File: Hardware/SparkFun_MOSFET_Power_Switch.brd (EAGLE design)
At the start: 38.1 x 35.6 mm, 75 parts, among them J1 PTH, J3 5.5x2.1mm Barrel, J4 SMD, Q1 600mA/40V, Q2 100A/100V/6.8mΩ, U1 LMR14203

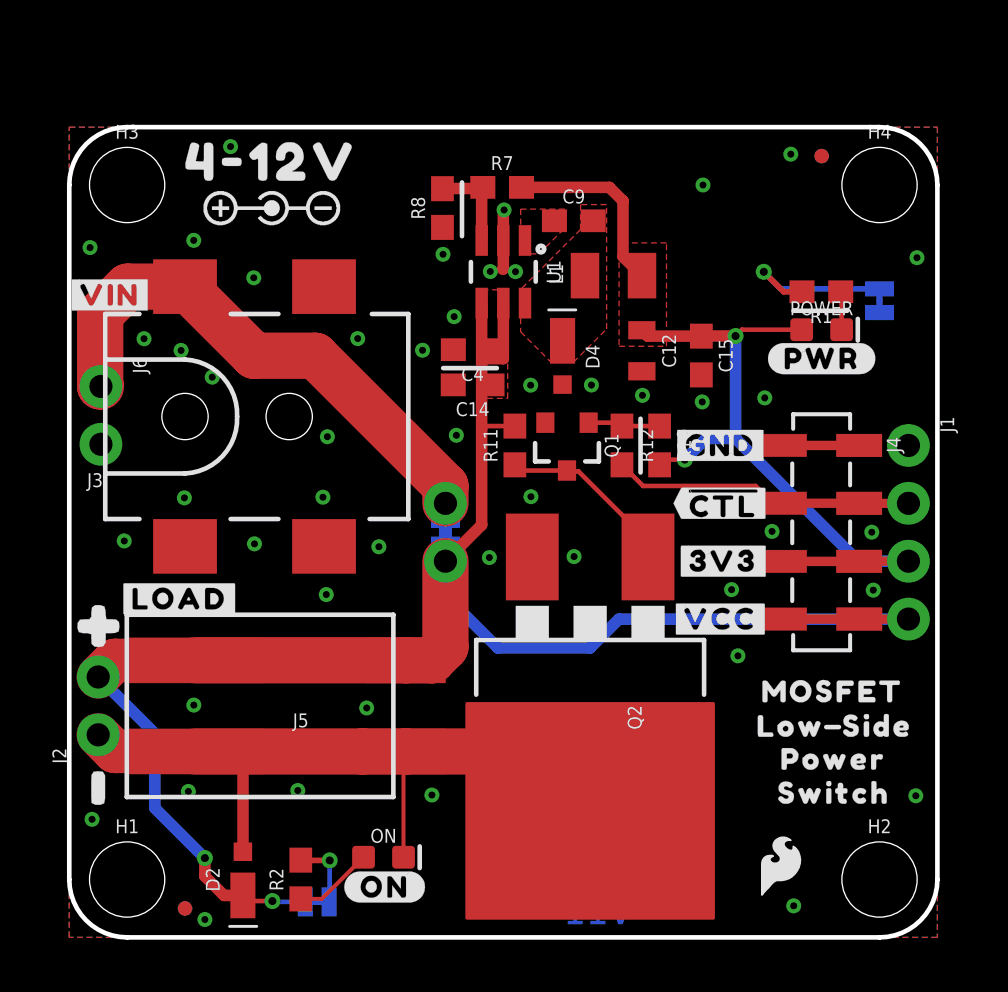
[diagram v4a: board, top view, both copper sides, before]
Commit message: Group Review mods round one
-Powered ON LED from 3.3V and controlled via CTL net.
-Moved GND/VIN PTH headers away from under the barrel jack for easier access
-routed some of load path with polygons to avoid sharp 90 degree turns in traces
-moved MEAS jumper to allow direct GND pour path from MOSFET to Barrel jack GND pads
-added "+" and "-" silk to MEAS jumper PTH header
-enlarged board to 1.5" square shape
-spaced out components near BJT for better DFM
-nudged some vias to avoid silk
-corrected voltage input range to "4.5-12V".
-added ordering instructions
-Larger logos
-added and updated measures
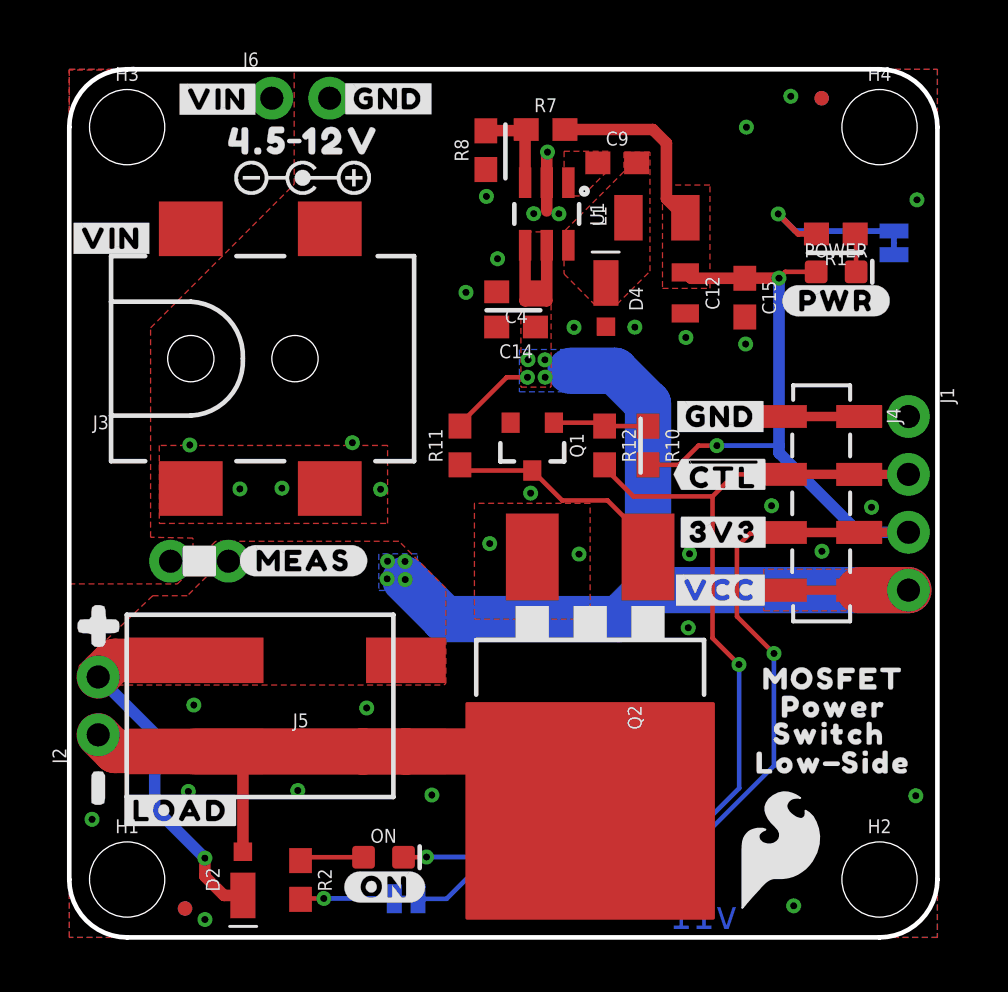
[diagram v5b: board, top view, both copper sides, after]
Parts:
- added LOGO3: SPECIAL_INSTRUCTIONS-ORDERING, SparkFun-Aesthetics:ORDERING_INSTRUCTIONS
- added U$18: (no value), output:4#5_12V5
- added U$21: (no value), output:#VIN#8
- added U$38: (no value), output:#MEAS#14
- LOGO1: value OSHW-LOGOS -> OSHW-LOGOM; device SparkFun-Aesthetics:OSHW-LOGO-S -> SparkFun-Aesthetics:OSHW-LOGO-M
- LOGO2: value SFE_LOGO_NAME_FLAME.1_INCH -> SFE_LOGO_NAME_FLAME.2_INCH; device SparkFun-Aesthetics:SFE_LOGO_NAME_FLAME_.1 -> SparkFun-Aesthetics:SFE_LOGO_NAME_FLAME_.2
- U$6: device output:4#12V0 -> output:#GND#0
- U$8: device SparkFun-Aesthetics:SFE_LOGO_FLAME_.1 -> SparkFun-Aesthetics:SFE_LOGO_FLAME_.2
- moved U$37 18.3 mm to (11.4, 34.3)
- moved U$34 15.1 mm to (15.7, 11.8)
- moved U$35 15.1 mm to (22.1, 11.9)
- moved J6 14.7 mm to (8.89, 36.8), turned to 0 degrees
- moved U$36 11.1 mm to (8.89, 34.5)
- moved MEAS 10.9 mm to (5.71, 16.5), turned to 180 degrees
- moved U$24 10.4 mm to (18.5, 18.7)
- moved LOGO2 9.52 mm to (18.8, 21.9)
- moved U$1 9.29 mm to (4.87, 5.57)
- moved U$17 9.17 mm to (5.74, 18.2), turned to 0 degrees
- moved U$26 8.26 mm to (18.8, 14.2)
- moved U$25 8.24 mm to (18.7, 16.6)
- moved LOGO1 5.92 mm to (33.9, 8.56)
- moved U$6 5.82 mm to (14.0, 36.8)
- moved U$16 3.95 mm to (19.4, 1.66)
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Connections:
- net !CTL: now also ON.C
- net 3.3V: now also ON_LED.2
- net LOAD: no longer ON.C
- net VCC: no longer ON_LED.2
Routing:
- net 3.3V: track 35.8 -> 73.5 mm, vias 2 -> 3
- net !CTL: track 15.4 -> 43.7 mm, vias 0 -> 2
- net VIN: track 24.0 -> 0.76 mm
- net VCC: track 78.2 -> 66.6 mm, vias 2 -> 9
- net LOAD: track 33.1 -> 28.4 mm
- net N$1: track 7.93 -> 10.3 mm
- net N$7: track 3.11 -> 4.14 mm
- net N$12: track 3.18 -> 4.19 mm
- net N$2: track 3.51 -> 2.83 mm
- net GND: track 2.63 -> 2.60 mm, vias 48 -> 35
- added copper zone on layer 16, net VCC
- added copper zone on layer 1, net VIN
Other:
- board size 38.1 x 35.6 mm -> 38.1 x 38.1 mm
- board text added: "2-Layer Design Soldermask: Red Silkscreen: White Thickness: 1.6mm Copper Plating: 2 OZ Surface Finish: Lead-Free HASL Material: TG135-140"

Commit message: BOM consolidation
-made the two 0.1uF caps the same one (100V).
-Enlarged LOAD net trace/connection with polygon.
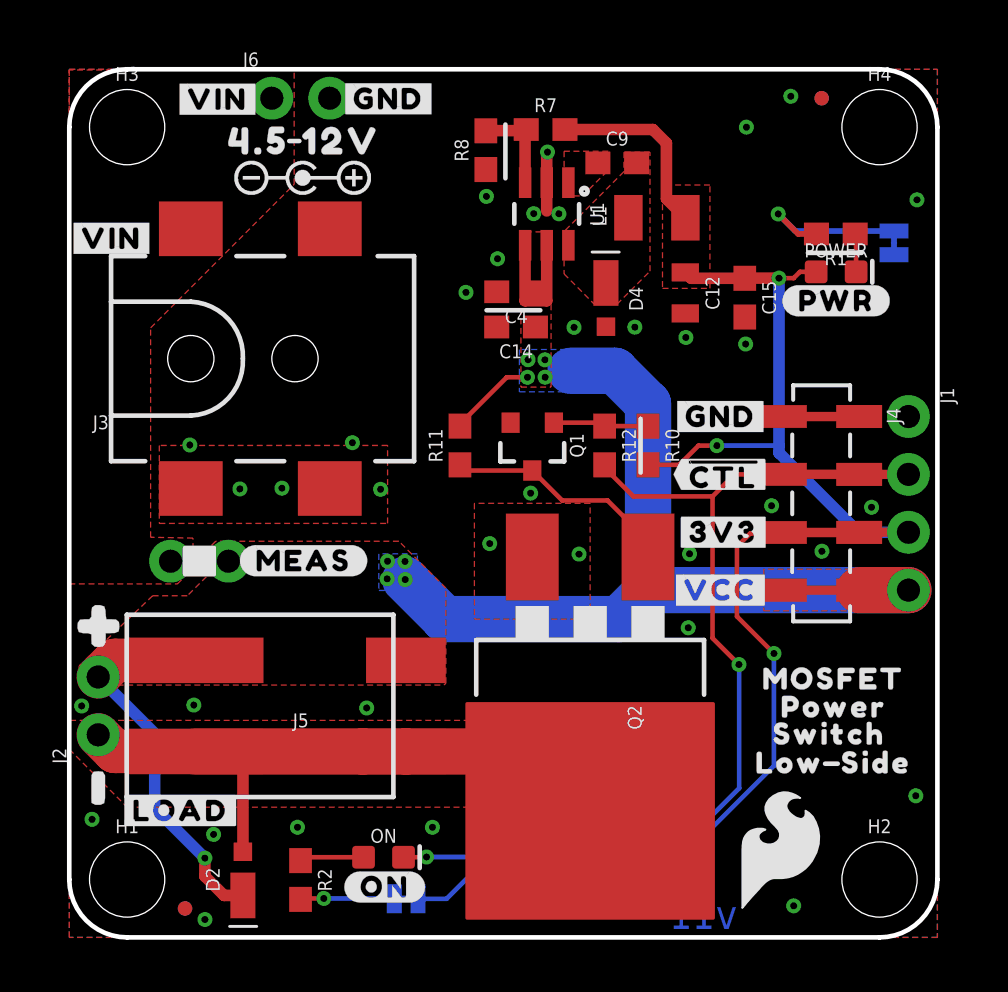
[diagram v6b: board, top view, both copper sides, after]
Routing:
- net GND: vias 35 -> 36
- added copper zone on layer 1, net LOAD
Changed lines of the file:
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@@
 <element name="C15" library="SparkFun-Capacitors" package="0603" value="0.1uF" x="29.646884375" y="28.0771625" smashed="yes" rot="R270">
 <attribute name="NAME" x="30.408884375" y="28.0771625" size="0.6096" layer="25" font="vector" ratio="20" rot="R270" align="bottom-center"/>
-<attribute name="PROD_ID" value="CAP-00810" x="15.676884375" y="35.6971625" size="1.778" layer="27" font="vector" ratio="15" rot="R270" display="off"/>
+<attribute name="PROD_ID" value="CAP-08390" x="15.676884375" y="35.6971625" size="1.778" layer="27" font="vector" ratio="15" rot="R270" display="off"/>
 <attribute name="VALUE" x="28.884884375" y="28.0771625" size="0.6096" layer="27" font="vector" ratio="20" rot="R270" align="top-center"/>
 </element>
@@
 <via x="13.053059375" y="10.068559375" extent="1-16" drill="0.3048"/>
 <via x="5.466078125" y="10.195559375" extent="1-16" drill="0.3048"/>
-<via x="15.9131" y="6.2484" extent="1-16" drill="0.3048"/>
+<via x="15.9385" y="4.831078125" extent="1-16" drill="0.3048"/>
 <via x="31.793178125" y="1.3843" extent="1-16" drill="0.3048"/>
 <via x="37.152578125" y="6.215378125" extent="1-16" drill="0.3048"/>
@@
 <via x="1.000759375" y="5.181596875" extent="1-16" drill="0.3048"/>
 <via x="5.953759375" y="0.78485625" extent="1-16" drill="0.3048"/>
-<via x="10.030459375" y="6.4465125" extent="1-16" drill="0.3048"/>
+<via x="10.01521875" y="4.8336125" extent="1-16" drill="0.3048"/>
 <via x="33.032696875" y="16.946884375" extent="1-16" drill="0.3048"/>
 <via x="27.165296875" y="13.58900625" extent="1-16" drill="0.3048"/>
@@
 <via x="9.3319625" y="19.715475" extent="1-16" drill="0.3048"/>
 <via x="13.662659375" y="19.664678125" extent="1-16" drill="0.3048"/>
-<via x="5.22731875" y="6.40333125" extent="1-16" drill="0.3048"/>
+<via x="6.33221875" y="4.518653125" extent="1-16" drill="0.3048"/>
 <polygon width="0.2032" layer="1" thermals="no">
 <vertex x="3.9522375" y="21.59"/>
@@
 <vertex x="22.86" y="13.97"/>
 </polygon>
+<via x="0.543559375" y="10.15745625" extent="1-16" drill="0.3048"/>
 </signal>
 <signal name="SDA1">
@@
 <wire x1="29.646884375" y1="28.9271625" x2="29.652859375" y2="28.9331375" width="0.508" layer="1"/>
 <wire x1="29.652859375" y1="28.9331375" x2="31.14801875" y2="28.9331375" width="0.508" layer="1"/>
-<wire x1="32.778" y1="29.21" x2="31.42488125" y2="29.21" width="0.2032" layer="1"/>
-<wire x1="31.42488125" y1="29.21" x2="31.14801875" y2="28.9331375" width="0.2032" layer="1"/>
+<wire x1="32.778" y1="29.21" x2="32.070040625" y2="29.21" width="0.2032" layer="1"/>
+<wire x1="32.070040625" y1="29.21" x2="31.793178125" y2="28.9331375" width="0.2032" layer="1"/>
+<wire x1="31.793178125" y1="28.9331375" x2="31.14801875" y2="28.9331375" width="0.2032" layer="1"/>
 <wire x1="28.4226" y1="21.58238125" x2="31.14801875" y2="21.58238125" width="0.2032" layer="16"/>
 <contactref element="ON_LED" pad="2"/>
@@
 <polygon width="0.2032" layer="1" thermals="no">
 <vertex x="0" y="15.51431875"/>
-<vertex x="4.745725" y="15.512015625"/>
 <vertex x="4.745725" y="15.512015625"/>
 <vertex x="5.429634375" y="16.195925"/>
@@
 <wire x1="7.62" y1="3.7592" x2="7.6230375" y2="3.7622375" width="0.508" layer="1"/>
 <wire x1="7.6230375" y1="7.76884375" x2="7.6230375" y2="3.7622375" width="0.508" layer="1"/>
+<polygon width="0.1524" layer="1" thermals="no">
+<vertex x="18.415" y="9.525"/>
+<vertex x="0" y="9.525"/>
+<vertex x="0" y="8.255"/>
+<vertex x="2.54" y="5.715"/>
+<vertex x="18.415" y="5.715"/>
+</polygon>
 </signal>
 <signal name="VCC">
